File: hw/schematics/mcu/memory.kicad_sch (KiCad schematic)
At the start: 2 parts

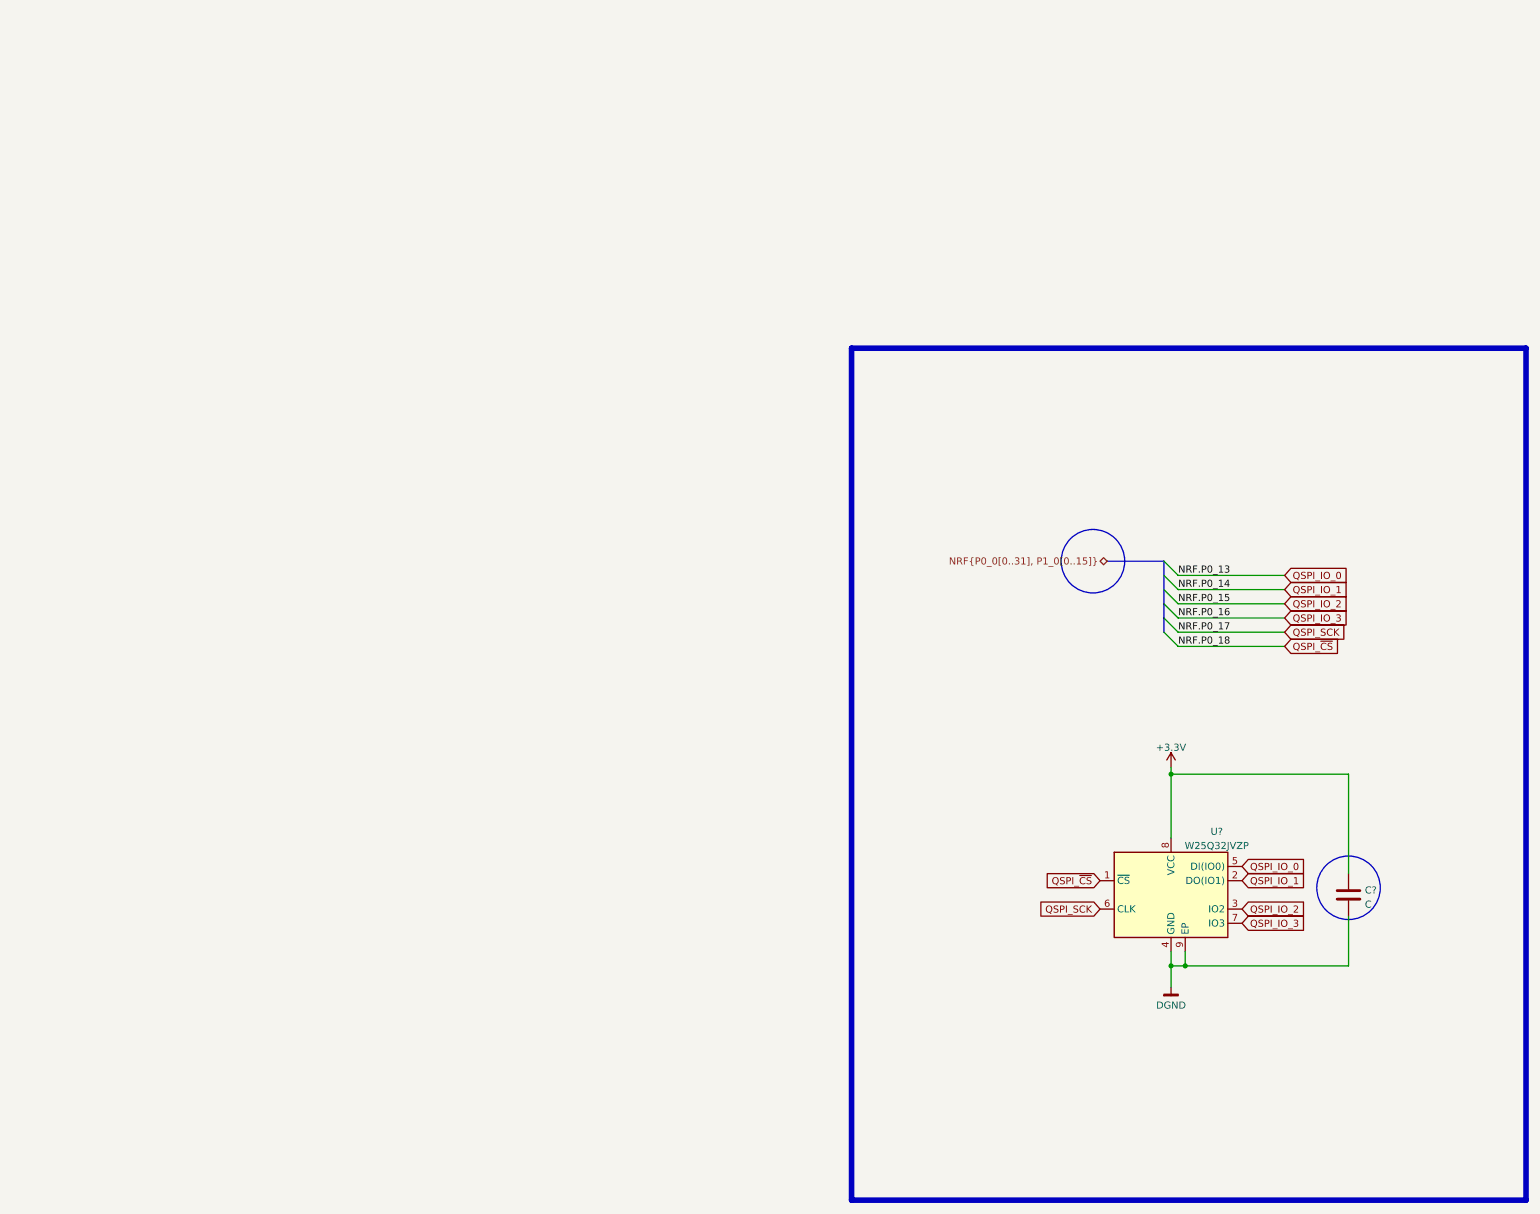
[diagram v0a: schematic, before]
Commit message: 
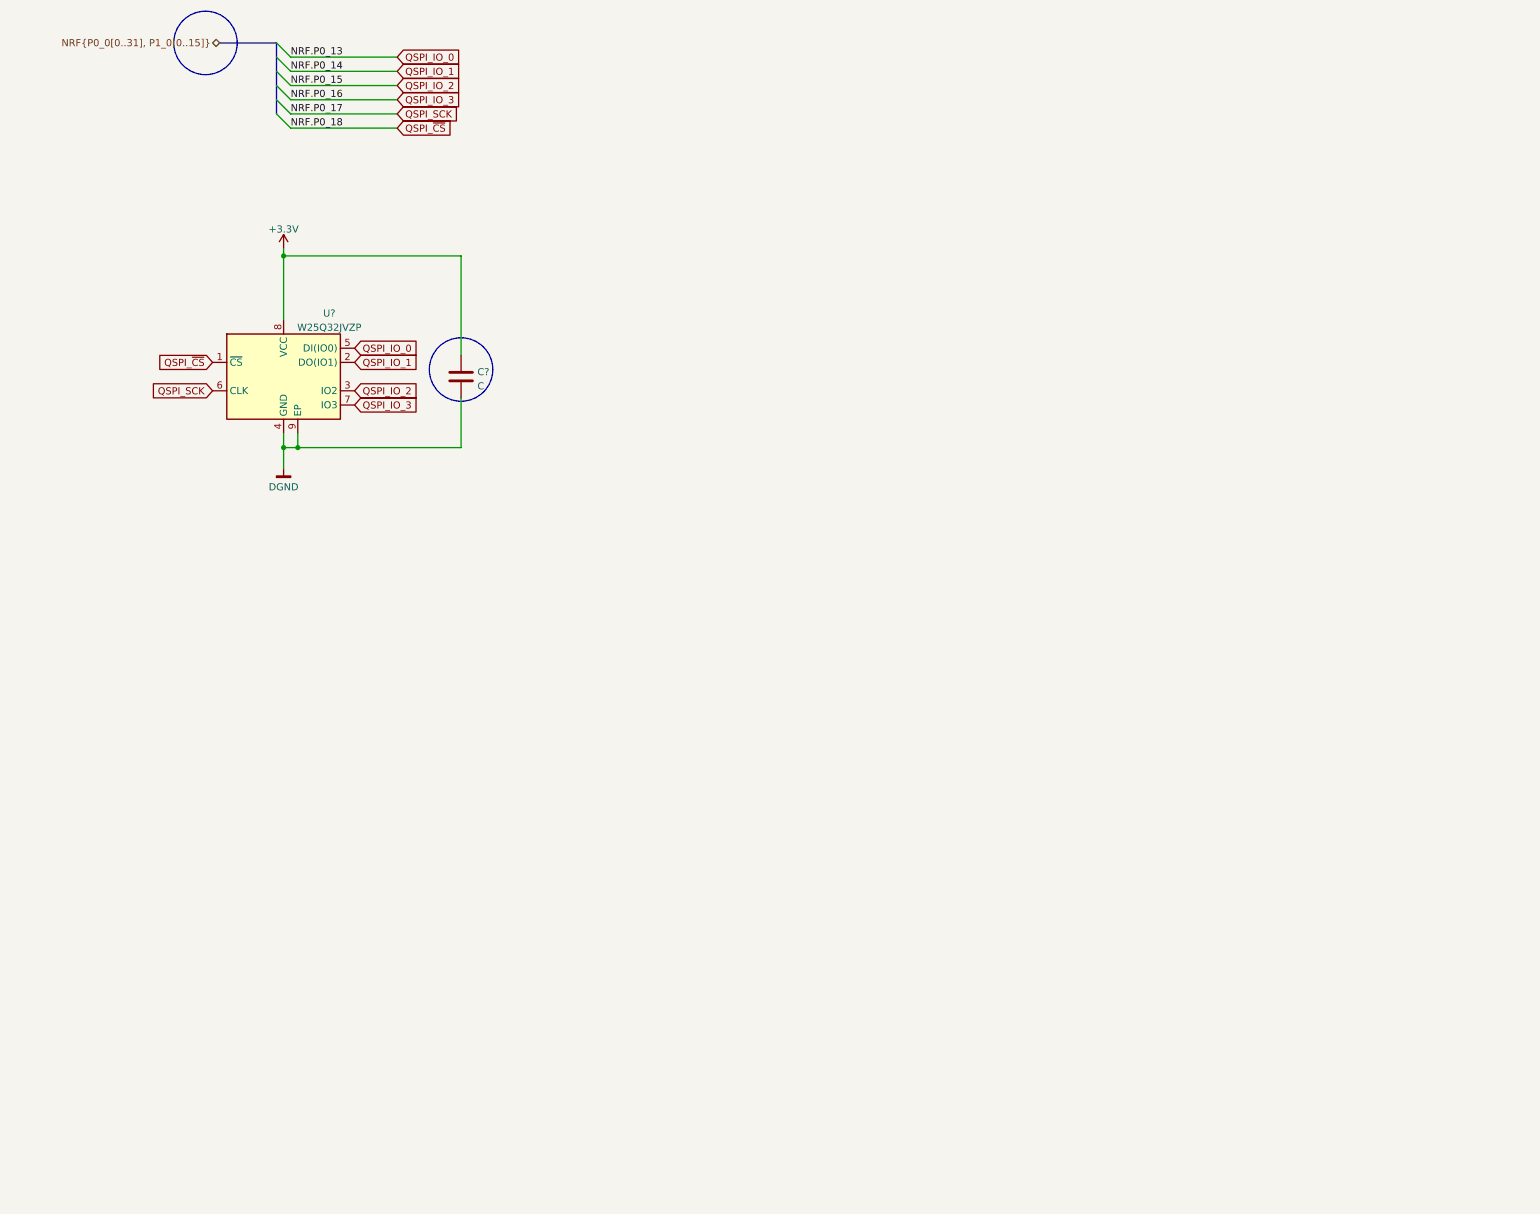
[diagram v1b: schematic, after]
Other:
- moved on the sheet: C?, U?
